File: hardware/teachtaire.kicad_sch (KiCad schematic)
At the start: 6 parts, among them U1 MAX-M10S, U2 STM32F072C8Tx, U3 SX1262IMLTRT, U4 TLV70433DBVT

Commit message: Finished Schematic and Routed PCB
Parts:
- removed U3: SX1262IMLTRT, Package_DFN_QFN:QFN-24-1EP_4x4mm_P0.5mm_EP2.6x2.6mm, symbol RF:SX1262IMLTRT
- added C22, C29: 4.7uF, Capacitor_SMD:C_0402_1005Metric, symbol Device:C
- added C23, C26, C27, C28, C30, C31, C36, C37, C39: 100nF, Capacitor_SMD:C_0402_1005Metric, symbol Device:C
- added C24, C38: 1uF, Capacitor_SMD:C_0402_1005Metric, symbol Device:C
- added C25: 10nF, Capacitor_SMD:C_0402_1005Metric, symbol Device:C
- added C32, C33: 8pF, Capacitor_SMD:C_0402_1005Metric, symbol Device:C
- added C34, C35: 47uF, Capacitor_SMD:C_0402_1005Metric, symbol Device:C
- added D2: NUP2105L, Package_TO_SOT_SMD:SOT-23, symbol Power_Protection:NUP2105L
- added D3: BAT54C, Package_TO_SOT_SMD:SOT-23, symbol Diode:BAT54C
- added J3: ESQ-110-X-X-D, SAMTEC_ESQ-110-14-G-D, symbol ESQ-110-X-X-D:ESQ-110-X-X-D
- added J4: XT30PW-M, footprints:AMASS_XT30PW-M, symbol XT30PW-M:XT30PW-M
- added J5: Conn_01x10, Connector_IDC:IDC-Header_2x05_P2.54mm_Vertical, symbol Connector_Generic:Conn_01x10
- added J6: Conn_Coaxial, Connector_Coaxial:SMA_BAT_Wireless_BWSMA-KWE-Z001, symbol Connector:Conn_Coaxial
- added MOSFET1: IPP80P03P4L04AKSA1, IPP80P03P4L04AKSA1, symbol IPP80P03P4L04AKSA1:IPP80P03P4L04AKSA1
- added R10, R9: 60 Ω, Resistor_SMD:R_0402_1005Metric, symbol Device:R
- added R8: 10kΩ, Resistor_SMD:R_0402_1005Metric, symbol Device:R
- added U10: radio_thing, radio_breakout:radio_breakout, symbol SX1261 - Copy:radio_thing
- added U3: TJA1051T/3/1J, SO8_SOT96-1_NXP, symbol TJA1051T:TJA1051T_3_1J
- added XTAL1: NX3225GD-8MHZ-STD-CRA-3, XTAL_NX3225GD-8MHZ-STD-CRA-3_NDK, symbol NX3225GD-8MHZ-STD-CRA-3:NX3225GD-8MHZ-STD-CRA-3
- D1: footprint (none) -> LED_SMD:LED_0402_1005Metric
- R1: footprint (none) -> Resistor_SMD:R_0402_1005Metric
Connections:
- net +3.3V: now also U2.1 (VBAT), U2.24 (VDD), U2.36 (VDDIO2), U2.48 (VDD), U2.9 (VDDA), C22.1, C23.1, C24.1, C25.1, C26.1, C27.1, C28.1, C29.1, C30.1, C37.1, C38.2, J5.7 (Pin_7), J5.8 (Pin_8), U10.3 (VCC), U3.5 (VIO)
- net GND: now also U2.23 (VSS), U2.35 (VSS), U2.47 (VSS), U2.8 (VSSA), U4.4 (NC), U4.5 (NC), C22.2, C23.2, C24.2, C25.2, C26.2, C27.2, C28.2, C29.2, C30.2, C31.2, C32.1, C33.1, C34.2, C35.2, C36.2, C38.1, C39.2, D2.3 (A), J3.03, J3.04, J3.07, J3.08, J3.14, J3.19, J3.20, J4.N, J5.5 (Pin_5), J5.6 (Pin_6), J6.2 (Ext), MOSFET1.1 (G), R8.1, U10.2 (GND), U3.2 (GND), U3.8 (S)
- net VBAT: now reaches U4.2 (IN)
- net VBAT: now also C39.1, D3.3
- net LoRa_RESET: now reaches U2.11 (PA1)
- net LoRa_RESET: now also U10.12 (RESET)
- net LoRa_NSS: now reaches U2.12 (PA2)
- net LoRa_NSS: now also U10.16 (nSEL)
- net LoRa_SCK: now reaches U2.15 (PA5)
- net LoRa_SCK: now also U10.13 (SCLK)
- net LoRa_MISO: now reaches U2.16 (PA6)
- net LoRa_MISO: now also U10.14 (SDO)
- net LoRa_MOSI: now reaches U2.17 (PA7)
- net LoRa_MOSI: now also U10.15 (SDI)
- net LoRa_RX_SWITCH: now reaches U2.29 (PA8)
- net LoRa_RX_SWITCH: now also U10.4 (RX_SWITCH)
- net CAN_-: now reaches U2.32 (PA11)
- net CAN_-: now also U3.4 (RXD)
- net CAN_+: now reaches U2.33 (PA12)
- net CAN_+: now also U3.1 (TXD)
- net SWDIO: now reaches U2.34 (PA13)
- net SWDIO: now also J3.15, J5.4 (Pin_4)
- net SWCLK1: now reaches U2.37 (PA14)
- net SWCLK1: now also J3.09, J5.2 (Pin_2)
- net LoRa_TX_SWITCH: now reaches U2.38 (PA15)
- net LoRa_TX_SWITCH: now also U10.5 (TX_SWITCH)
- net at U2.44 (BOOT0): now also R8.2
- net GNSS_RESET: now reaches U2.45 (PB8)
- net GNSS_RESET: now also U1.9 (~{RESET})
- net at U2.5 (PF0): now also C32.2, XTAL1.1
- net at U2.6 (PF1): now also C33.2, XTAL1.2
- net NRST: now reaches U2.7 (NRST)
- net NRST: now also C31.1, J3.17, J5.1 (Pin_1)
- net GNSS_Bias_T/RF_IN: now reaches U1.11 (RF_IN)
- net GNSS_Bias_T/ANT_OFF_N: now reaches U1.13 (LNA_EN)
- net GNSS_Bias_T/ANT_DETECT: now reaches U1.16 (SDA)
- net GNSS_Bias_T/ANT_SHORT_N: now reaches U1.17 (SCL)
- new net: J4.P, MOSFET1.2 (D)
- new net: C34.1, R10.2, R9.1
- new net: J6.1 (In), U10.1 (Antenna)
- new net: D3.2, MOSFET1.3 (S)
- new net 5VLOGIC: C35.1, C36.1, C37.2, D3.1, J3.05, J3.06, U3.3 (VCC)
- new net 5VSERVO: J3.01, J3.02
- new net CANo_+: D2.1 (K), J3.16, R10.1, U3.7 (CANH)
- new net CANo_-: D2.2 (K), J3.18, R9.2, U3.6 (CANL)
- no-connect marks 0 -> 31
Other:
- removed sheet LoRa
- sheet GNSS_Bias_T ports: added ANT_DETECT, ANT_OFF_N, ANT_SHORT_N, Antenna Supply, RF_IN, V_ANT; removed none
- moved on the sheet: D1, R1, U1, U2, U4

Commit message: minorest of changes
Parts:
- removed U10: radio_thing, radio_breakout:radio_breakout, symbol SX1261 - Copy:radio_thing
- added U8: RF-LORA-868-SO, XCVR_RF-LORA-868-SO, symbol RF-LORA-868-SO:RF-LORA-868-SO
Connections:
- net +3.3V: now also U8.3 (VCC)
- net GND: now also U8.2 (GND)
- net LoRa_MISO: now also U8.14 (SDO)
- net LoRa_MOSI: now also U8.15 (SDI)
- net LoRa_NSS: now also U8.16 (~{SEL})
- net LoRa_RESET: now also U8.12 (RESET)
- net LoRa_RX_SWITCH: now also U8.4 (RX_SWITCH)
- net LoRa_SCK: now also U8.13 (SCLK)
- net LoRa_TX_SWITCH: now also U8.5 (TX_SWITCH)
- net at J6.1 (In): now also U8.1 (ANT)
- net GNSS_Bias_T/Antenna Supply: now reaches U1.14 (VCC_RF)
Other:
- note added: "should this be pulled to a known state?"
- moved on the sheet: C38, C39, D1, D3, J4, J6, MOSFET1, R1, U1, U4

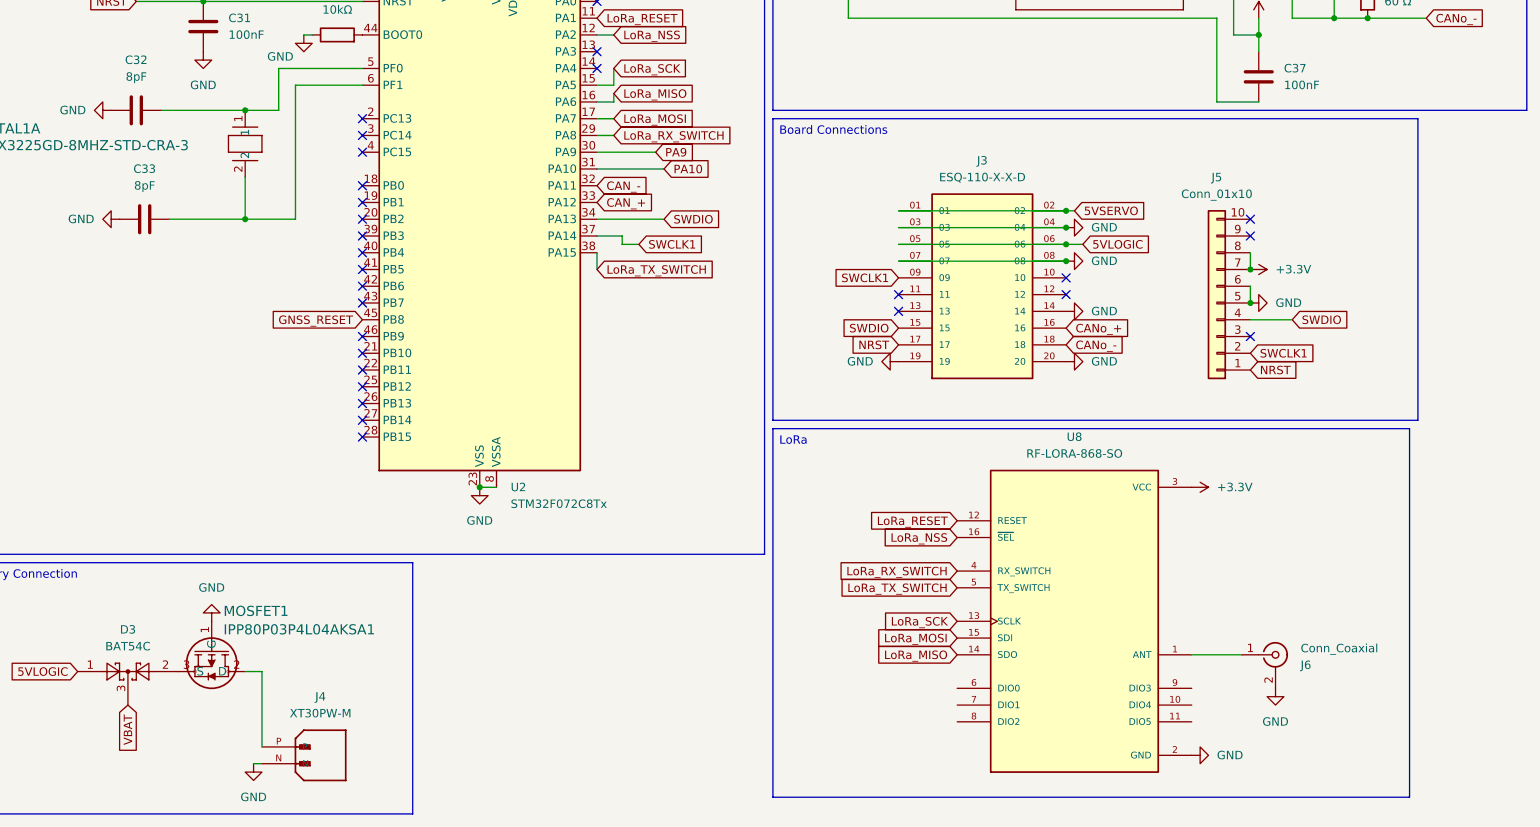
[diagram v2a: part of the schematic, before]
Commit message: Changes from Reddit review 1
Changed connector, impedance matched the RF traces, changed board to square
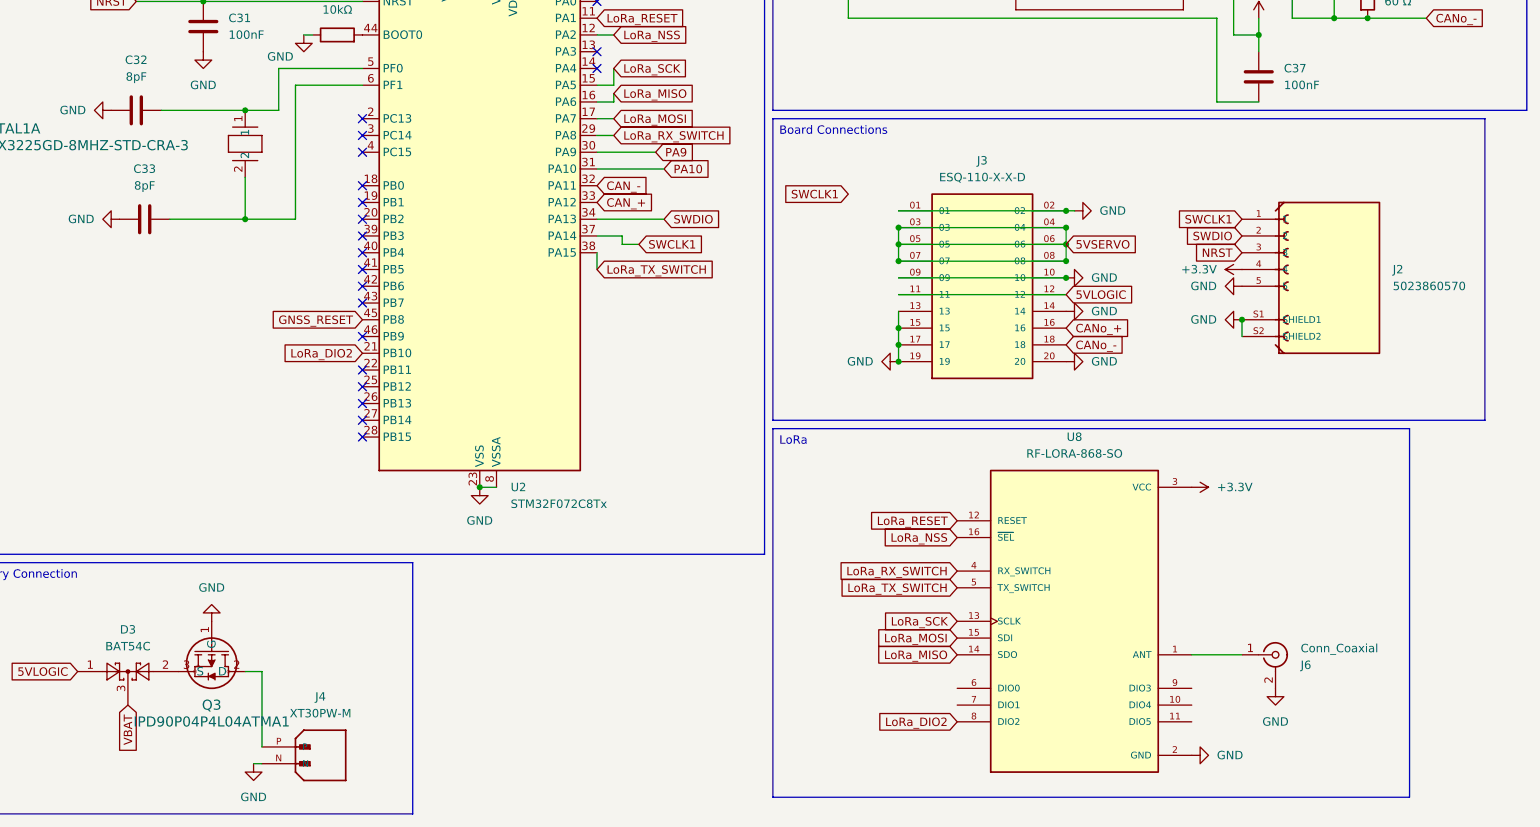
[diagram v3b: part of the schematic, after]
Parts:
- removed J5: Conn_01x10, Connector_IDC:IDC-Header_2x05_P2.54mm_Vertical, symbol Connector_Generic:Conn_01x10
- removed MOSFET1: IPP80P03P4L04AKSA1, IPP80P03P4L04AKSA1, symbol IPP80P03P4L04AKSA1:IPP80P03P4L04AKSA1
- added J2: 5023860570, MOLEX_5023860570, symbol 5023860570:5023860570
- added Q3: IPD90P04P4L04ATMA1, PG-TO252-3-313_INF-L, symbol IPD90P04P4L04ATMA1:IPD90P04P4L04ATMA1
- U4: footprint DBV0005A_N -> DBV0005A_L
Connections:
- net +3.3V: now also J2.4
- net 5VLOGIC: now also J3.11, J3.12; no longer J3.05, J3.06
- net 5VSERVO: now also J3.03, J3.04, J3.05, J3.06, J3.07, J3.08; no longer J3.01, J3.02
- net GND: now also J3.01, J3.02, J3.09, J3.10, J3.13, J3.15, J3.17, J2.5, J2.S1 (SHIELD1), J2.S2 (SHIELD2), Q3.1 (G); no longer J3.03, J3.04, J3.07, J3.08
- net NRST: now also J2.3; no longer J3.17
- net SWCLK1: now also J2.1; no longer J3.09
- net SWDIO: now also J2.2; no longer J3.15
- net LoRa_DIO2: now reaches U8.8 (DIO2)
- net LoRa_DIO2: now also U2.21 (PB10)
- net at J4.P: now also Q3.2 (D)
- net at D3.2: now also Q3.3 (S)
- no-connect marks 31 -> 23

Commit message: many fatal fuck-ups found
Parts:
- removed C38: 1uF, Capacitor_SMD:C_0402_1005Metric, symbol Device:C
- removed C39: 100nF, Capacitor_SMD:C_0402_1005Metric, symbol Device:C
- removed J4: XT30PW-M, footprints:AMASS_XT30PW-M, symbol XT30PW-M:XT30PW-M
- removed U4: TLV70433DBVT, DBV0005A_L, symbol TLV70433DBVT:TLV70433DBVT
- added C11, C13: 4.7uF, Capacitor_SMD:C_0402_1005Metric, symbol Device:C
- added C12, C14: 100nF, Capacitor_SMD:C_0402_1005Metric, symbol Device:C
- added GND1, VBCKP1: TestPoint, TestPoint:TestPoint_Pad_D2.0mm, symbol Connector:TestPoint
- added J4: 39-29-1048, MOLEX_39-29-1048, symbol 39-29-1048:39-29-1048
- added Q4: NMOS, Package_TO_SOT_SMD:SOT-23, symbol Simulation_SPICE:NMOS
- added R11: 10kΩ, Resistor_SMD:R_0402_1005Metric, symbol Device:R
- R10, R9: value 60 Ω -> 60Ω
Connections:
- net +3.3V: now also R1.1; no longer C22.1, C23.1, C24.1, C25.1, C26.1, C27.1, C28.1, C29.1, C30.1, C37.1, U1.7 (VCC_IO), U1.8 (VCC), U2.1 (VBAT), U2.24 (VDD), U2.36 (VDDIO2), U2.48 (VDD), U2.9 (VDDA), U3.5 (VIO), U8.3 (VCC)
- net 5VLOGIC: now also C37.1; no longer C37.2
- net GND: now also C11.1, C12.1, C13.2, C14.2, GND1.1, J4.3, J4.4, Q4.3 (S); no longer D1.1 (K)
- net at Q3.2 (D): now also J4.1, J4.2
- net at U1.4 (TIMEPULSE): now also Q4.2 (G), R11.2; no longer R1.1
- net at U1.6 (V_BCKP): now also VBCKP1.1
- net SWCLK1 renamed SWCLK
- new net: D1.1 (K), Q4.1 (D)
- new net +3V3D: C22.1, C23.1, C24.1, C25.1, C26.1, C27.1, C28.1, C29.1, C30.1, C37.2, R11.1, U2.1 (VBAT), U2.24 (VDD), U2.36 (VDDIO2), U2.48 (VDD), U2.9 (VDDA), U3.5 (VIO)
- new net +3V3RF: C11.2, C12.2, C13.1, C14.1, U1.7 (VCC_IO), U1.8 (VCC), U8.3 (VCC)
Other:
- added sheet power (power.kicad_sch)
- note removed: "should this be pulled to a known state?"
- moved on the sheet: C35, C36, C37, D1, D2, D3, Q3, R1, U1, XTAL1A

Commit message: fixed the fuck-ups
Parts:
- added D4: BAT54J, Diode_SMD:D_SOD-323F, symbol Diode:BAT54J
- renumbered C11 to C1, C26 to C10, C24 to C11, C25 to C12, C22 to C13, C23 to C14, C35 to C15, C36 to C16, C37 to C17, C13 to C18, C14 to C19, C12 to C2, C34 to C20, C29 to C3, C30 to C4, C32 to C5, C33 to C6, C31 to C7, C28 to C8, C27 to C9, D3 to D2, D2 to D3, J4 to J1, J3 to J2, J6 to J3, J2 to J4, Q4 to Q1, Q3 to Q2, R11 to R1, R1 to R2, R8 to R3, R10 to R4, R9 to R5, U8 to U4
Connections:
- net at U1.6 (V_BCKP): now also D4.1 (K); no longer VBCKP1.1
- new net: D4.2 (A), VBCKP1.1
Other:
- sheet power ports: added 3V3D, 3V3RF; removed 3.3v
- moved on the sheet: GND1, VBCKP1

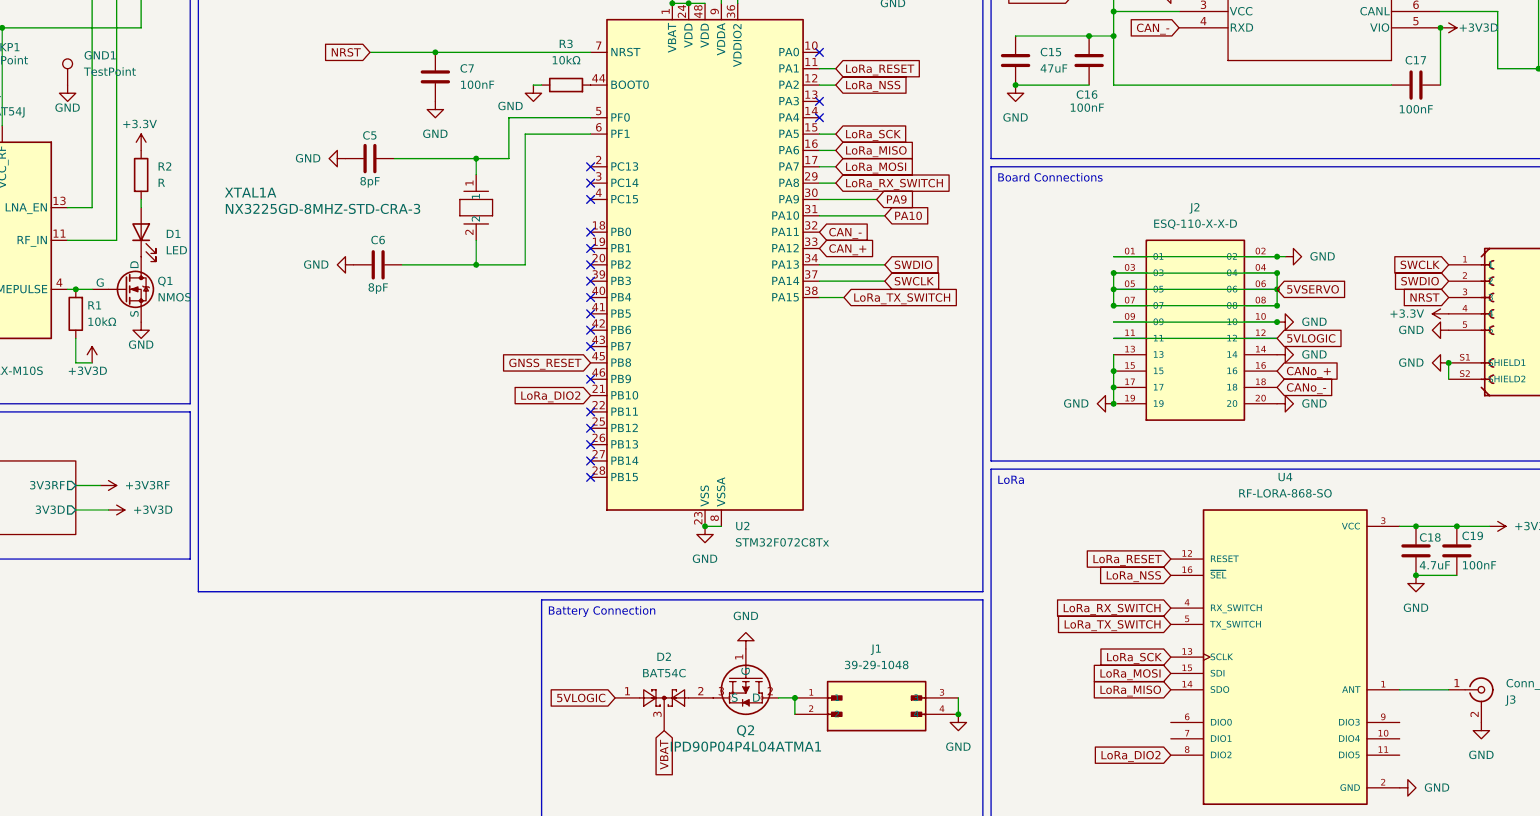
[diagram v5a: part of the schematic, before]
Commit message: power and main routing done, just need to set rf trace width
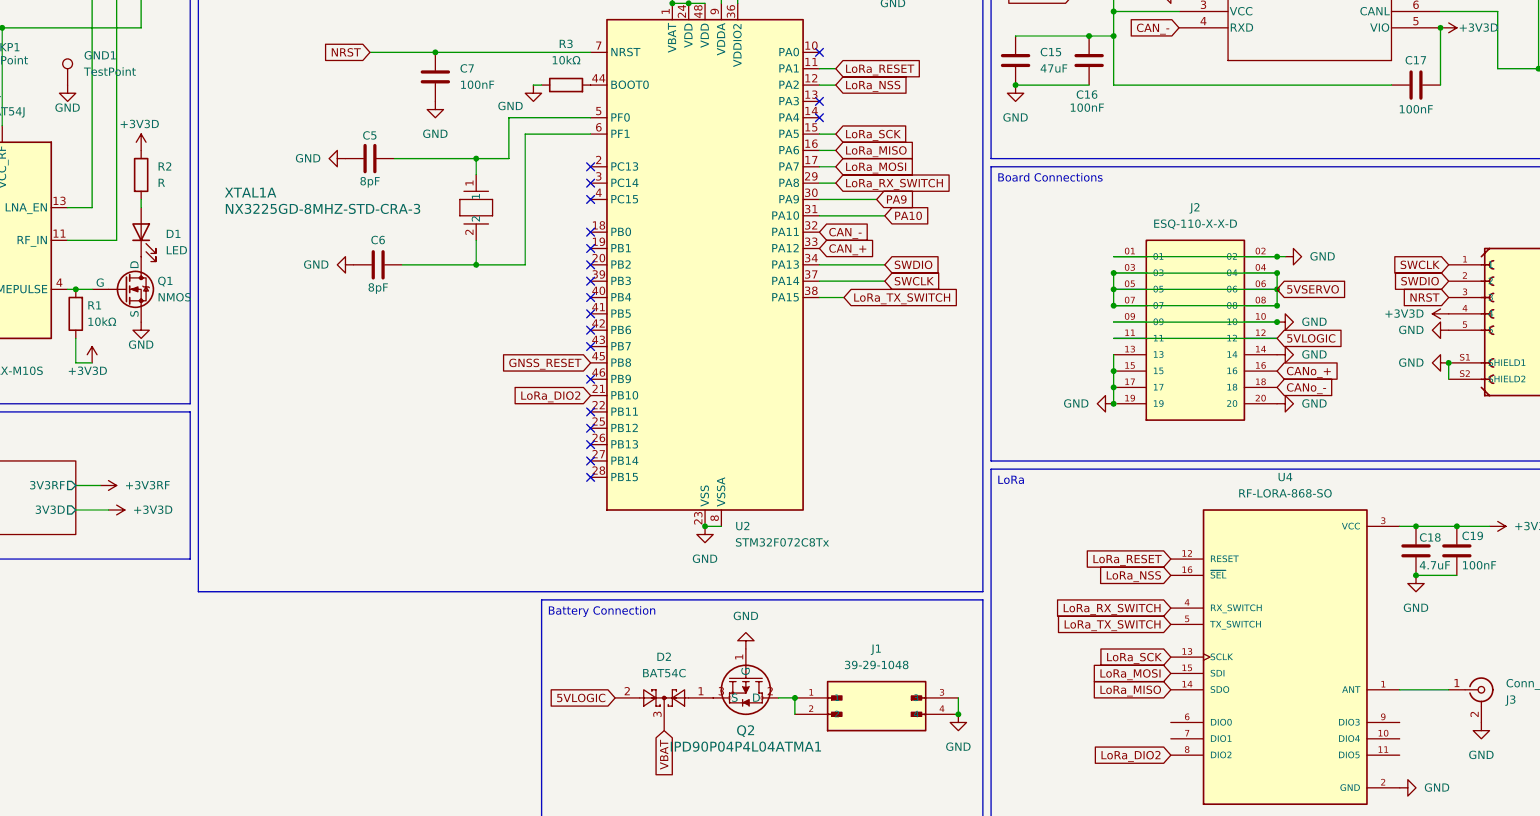
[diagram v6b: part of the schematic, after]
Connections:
- net +3.3V is gone; now on net +3V3D: J4.4, R2.1
- net 5VLOGIC: now also D2.2; no longer D2.1
- net at Q2.3 (S): now also D2.1; no longer D2.2
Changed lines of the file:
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@@
 			)
 		)
-		(property "Value" "+3.3V"
+		(property "Value" "+3V3D"
 			(at 96.266 68.326 0)
 			(effects
@@
 			)
 		)
-		(property "Value" "+3.3V"
+		(property "Value" "+3V3D"
 			(at 295.91 97.7899 90)
 			(effects
@@
 		(lib_id "Diode:BAT54C")
 		(at 177.8 157.48 0)
-		(unit 1)
-		(exclude_from_sim no)
-		(in_bom yes)
-		(on_board yes)
-		(dnp no)
-		(fields_autoplaced yes)
+		(mirror y)
+		(unit 1)
+		(exclude_from_sim no)
+		(in_bom yes)
+		(on_board yes)
+		(dnp no)
 		(property "Reference" "D2"
 			(at 177.8 151.13 0)
@@
 		)
 		(property "Footprint" "Package_TO_SOT_SMD:SOT-23"
-			(at 179.705 154.305 0)
+			(at 175.895 154.305 0)
 			(effects
 				(font
@@
 		)
 		(property "Datasheet" "http://www.diodes.com/_files/datasheets/ds11005.pdf"
-			(at 175.768 157.48 0)
-			(effects
-				(font
+			(at 179.832 157.48 0)
+			(effects
+				(font

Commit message: good to go
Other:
- note added: "50 Coplanar Single Ended L 1 / L 2 0.1565mm / 0.5080mm"
- note added: "JLC06061H-3313(Standard/Finished thickness0.57±0.10mm)"
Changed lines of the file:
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@@
 	(generator_version "9.0")
 	(paper "A3")
+	(text "50\nCoplanar Single Ended\nL\n1\n/\nL\n2\n0.1565mm\n/\n0.5080mm"
+		(exclude_from_sim no)
+		(at 72.136 156.718 0)
+		(effects
+			(font
+				(size 1.27 1.27)
+			)
+		)
+	)
+	(text "JLC06061H-3313(Standard/Finished thickness0.57±0.10mm)"
+		(exclude_from_sim no)
+		(at 119.634 152.146 0)
+		(effects
+			(font
+				(size 1.27 1.27)
+			)
+		)
+	)
 	(text_box "Board Connections"
 		(exclude_from_sim no)

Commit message: ddio pins
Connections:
- net LoRa_DIO2: now also U2.25 (PB12); no longer U2.21 (PB10)
- net LoRa_DIO4: now reaches U4.10 (DIO4)
- net LoRa_DIO4: now also U2.27 (PB14)
- net LoRa_DIO5: now reaches U4.11 (DIO5)
- net LoRa_DIO5: now also U2.28 (PB15)
- net LoRa_DIO0: now reaches U4.6 (DIO0)
- net LoRa_DIO0: now also U2.21 (PB10)
- net LoRa_DIO1: now reaches U4.7 (DIO1)
- net LoRa_DIO1: now also U2.22 (PB11)
- net LoRa_DIO3: now reaches U4.9 (DIO3)
- net LoRa_DIO3: now also U2.26 (PB13)
- no-connect marks 23 -> 18
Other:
- note added: "50Ω Coplanar Single Ended L1/L2 0.1565mm - trace width 0.5080mm - distance between top layer gnd pours and traces"
- note removed: "50 Coplanar Single Ended L 1 / L 2 0.1565mm / 0.5080mm"
- moved on the sheet: J3
